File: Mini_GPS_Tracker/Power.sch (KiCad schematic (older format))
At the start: 8 parts, among them J2 Screw_Terminal_01x02, SW2 MLL1200S, U3 LD1117S33TR_SOT223

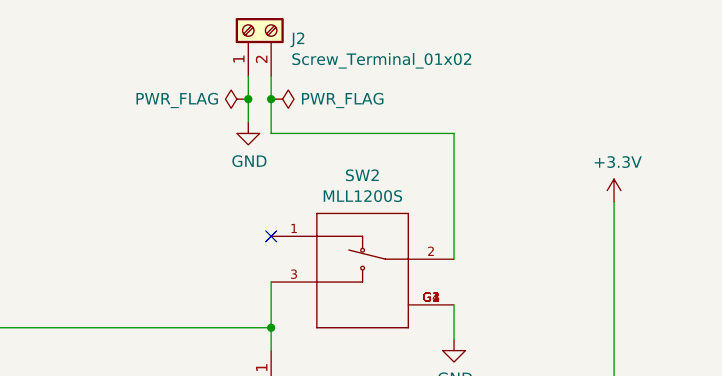
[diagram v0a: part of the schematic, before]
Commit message: Add files via upload
Splitting board into modules
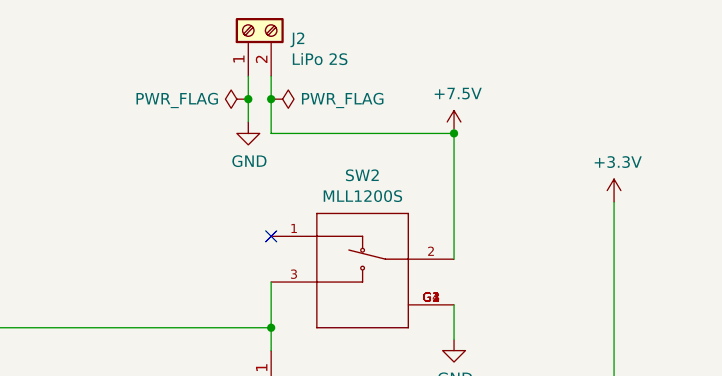
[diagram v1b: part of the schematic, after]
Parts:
- J2: value Screw_Terminal_01x02 -> LiPo 2S
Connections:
- net +7.5V: now reaches J2.2 (Pin_2), SW2.2
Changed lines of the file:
@@
 $Descr A4 11693 8268
 encoding utf-8
-Sheet 3 7
+Sheet 3 13
 Title ""
 Date ""
@@
 P 5150 1700
 F 0 "J2" V 5114 1512 50  0000 R CNN
-F 1 "Screw_Terminal_01x02" V 5023 1512 50  0000 R CNN
+F 1 "LiPo 2S" V 5023 1512 50  0000 R CNN
 F 2 "Connector_AMASS:AMASS_XT30UPB-F_1x02_P5.0mm_Vertical" H 5150 1700 50  0001 C CNN
 F 3 "~" H 5150 1700 50  0001 C CNN
@@
 	1    0    0    -1
 $EndComp
+$Comp
+L power:+7.5V #PWR052
+U 1 1 5EB2F129
+P 6050 2150
+F 0 "#PWR052" H 6050 2000 50  0001 C CNN
+F 1 "+7.5V" H 6065 2323 50  0000 C CNN
+F 2 "" H 6050 2150 50  0001 C CNN
+F 3 "" H 6050 2150 50  0001 C CNN
+	1    6050 2150
+	1    0    0    -1
+$EndComp
+Connection ~ 6050 2150
 $EndSCHEMATC
